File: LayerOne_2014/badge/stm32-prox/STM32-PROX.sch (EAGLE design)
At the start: 192 parts, among them IC1 IC_TPS6120X-QFN10, IC10 74XX244-OCTAL-TRISTATE-BUFFERS, IC105 MCP1824T-250, IC106 MCP1824T-120, IC11 CD4066, IC13 PQ1X331M2ZP-3V3-LDO-SOT-23-5, IC14 AD8052, IC2 STM32F103RET6, IC3 PQ1X331M2ZP-3V3-LDO-SOT-23-5, IC4 HCU-INVERTER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

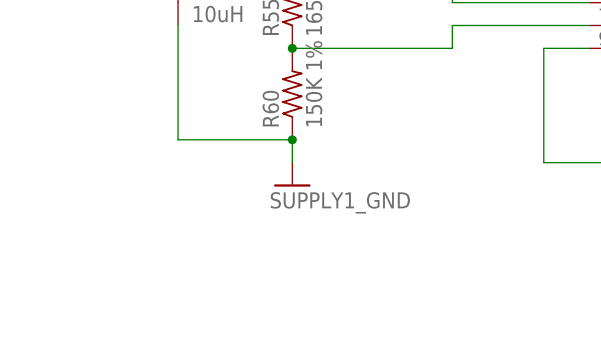
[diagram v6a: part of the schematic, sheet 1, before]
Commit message: 
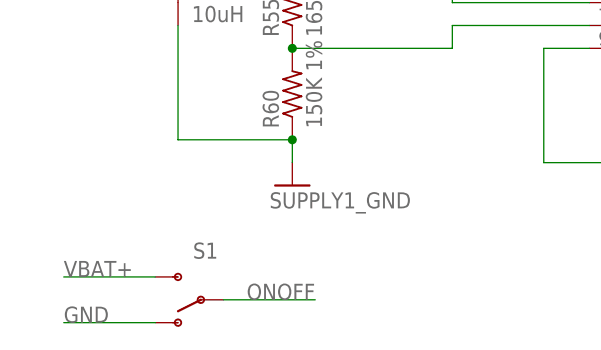
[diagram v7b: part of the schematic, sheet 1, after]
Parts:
- added S1: (no value), SparkFun-Electromechanical:SWITCH-SPDT-SMD-A
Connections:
- net GND: now also S1.O
- net ONOFF: now also S1.P
- net VBAT+: now also S1.S
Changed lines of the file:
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@@
 <part name="U$9" library="STM32-PROX" deviceset="BATT" device=""/>
 <part name="TP10" library="STM32-PROX" deviceset="--MERGED_TESTPAD" device="KEYSTONE-SMD" value="--MERGED_TESTPADKEYSTONE-SMD"/>
+<part name="S1" library="SparkFun-Electromechanical" deviceset="SWITCH-SPDT" device="-SMD-A"/>
 </parts>
 <sheets>
@@
 <instance part="U$9" gate="G$1" x="99.06" y="66.04"/>
 <instance part="TP10" gate="G$1" x="40.64" y="17.78"/>
+<instance part="S1" gate="1" x="-58.42" y="-25.4" rot="R180"/>
 </instances>
 <busses>
@@
 <wire x1="99.06" y1="60.96" x2="99.06" y2="53.34" width="0.1524" layer="91"/>
 <label x="101.6" y="55.88" size="1.778" layer="95"/>
+</segment>
+<segment>
+<pinref part="S1" gate="1" pin="S"/>
+<wire x1="-63.5" y1="-22.86" x2="-73.66" y2="-22.86" width="0.1524" layer="91"/>
+<label x="-73.66" y="-22.86" size="1.778" layer="95"/>
 </segment>
 </net>
@@
 <junction x="-48.26" y="-7.62"/>
 </segment>
+<segment>
+<pinref part="S1" gate="1" pin="O"/>
+<wire x1="-63.5" y1="-27.94" x2="-73.66" y2="-27.94" width="0.1524" layer="91"/>
+<label x="-73.66" y="-27.94" size="1.778" layer="95"/>
+</segment>
 </net>
 <net name="VBAT-" class="0">
@@
 <label x="-25.4" y="10.16" size="1.778" layer="95"/>
 </segment>
-</net>
+<segment>
+<pinref part="S1" gate="1" pin="P"/>
+<wire x1="-55.88" y1="-25.4" x2="-45.72" y2="-25.4" width="0.1524" layer="91"/>
+<label x="-53.34" y="-25.4" size="1.778" layer="95"/>
+</segment>
+</net>

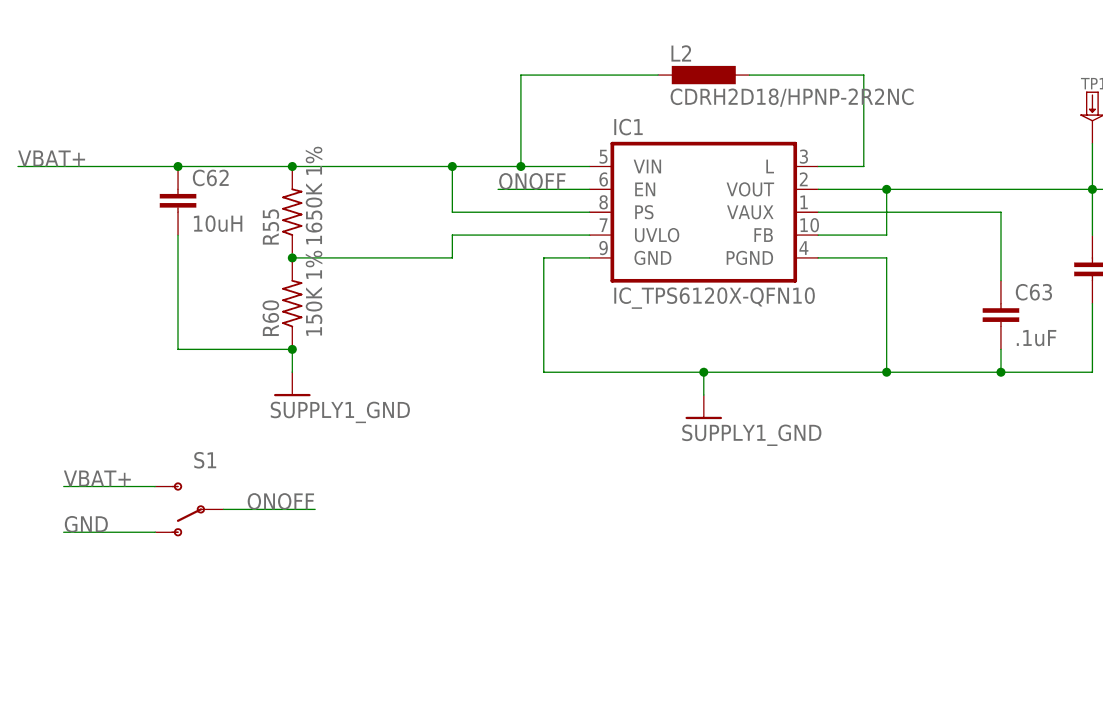
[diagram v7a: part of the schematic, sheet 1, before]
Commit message: 
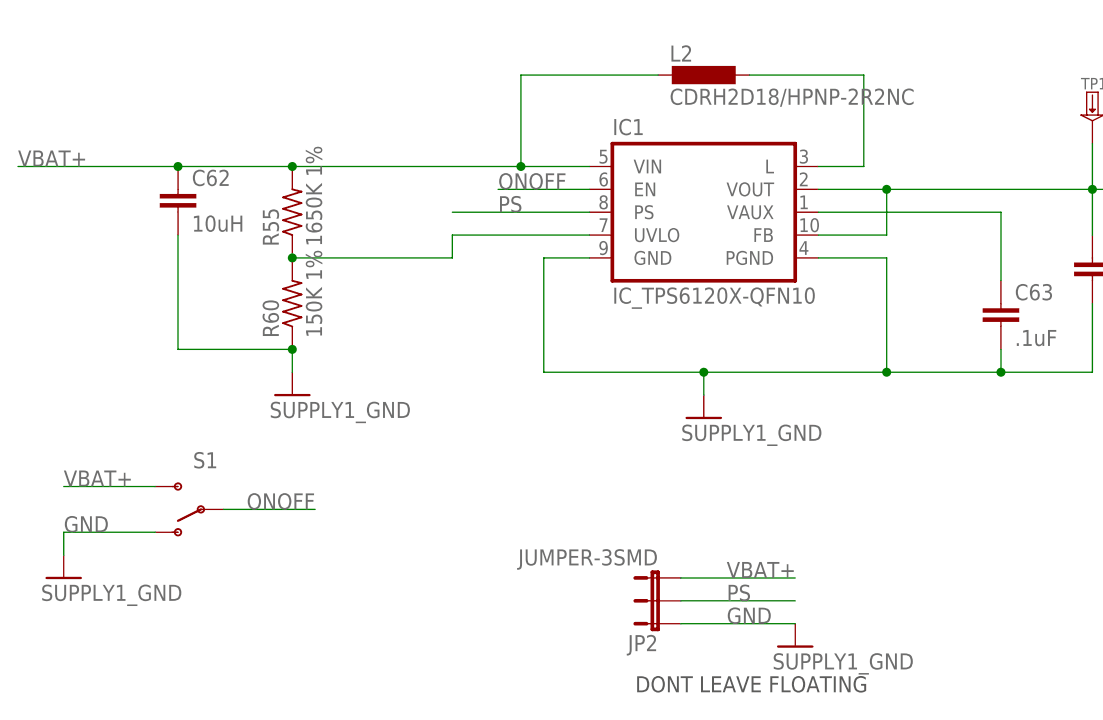
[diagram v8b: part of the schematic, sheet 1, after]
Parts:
- added JP2: JUMPER-3SMD, SparkFun-Passives:JUMPER-3SMD
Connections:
- new net PS: IC1IC.PS, JP2.2
- net GND: now also JP2.1
- net VBAT+: now also JP2.3; no longer IC1IC.PS
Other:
- note added: "DONT LEAVE FLOATING"
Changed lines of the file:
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@@
 <part name="TP10" library="STM32-PROX" deviceset="--MERGED_TESTPAD" device="KEYSTONE-SMD" value="--MERGED_TESTPADKEYSTONE-SMD"/>
 <part name="S1" library="SparkFun-Electromechanical" deviceset="SWITCH-SPDT" device="-SMD-A"/>
+<part name="GND20" library="badge.lbrbadge_2013" deviceset="SUPPLY1_GND" device=""/>
+<part name="JP2" library="SparkFun-Passives" deviceset="JUMPER-3" device="SMD"/>
+<part name="GND21" library="badge.lbrbadge_2013" deviceset="SUPPLY1_GND" device=""/>
 </parts>
 <sheets>
 <sheet>
 <plain>
+<text x="-10.16" y="-45.72" size="1.778" layer="97">DONT LEAVE FLOATING</text>
 </plain>
 <instances>
@@
 <instance part="TP10" gate="G$1" x="40.64" y="17.78"/>
 <instance part="S1" gate="1" x="-58.42" y="-25.4" rot="R180"/>
+<instance part="GND20" gate="1" x="-73.66" y="-33.02"/>
+<instance part="JP2" gate="G$1" x="-7.62" y="-38.1" rot="R90"/>
+<instance part="GND21" gate="1" x="7.62" y="-40.64"/>
 </instances>
 <busses>
@@
 <wire x1="-60.96" y1="12.7" x2="-78.74" y2="12.7" width="0.1524" layer="91"/>
 <junction x="-60.96" y="12.7"/>
-<pinref part="IC1" gate="IC" pin="PS"/>
-<wire x1="-15.24" y1="7.62" x2="-30.48" y2="7.62" width="0.1524" layer="91"/>
-<wire x1="-30.48" y1="7.62" x2="-30.48" y2="12.7" width="0.1524" layer="91"/>
-<junction x="-30.48" y="12.7"/>
 <pinref part="R55" gate="G$1" pin="2"/>
 <junction x="-48.26" y="12.7"/>
@@
 <wire x1="-63.5" y1="-22.86" x2="-73.66" y2="-22.86" width="0.1524" layer="91"/>
 <label x="-73.66" y="-22.86" size="1.778" layer="95"/>
+</segment>
+<segment>
+<pinref part="JP2" gate="G$1" pin="3"/>
+<wire x1="-5.08" y1="-33.02" x2="7.62" y2="-33.02" width="0.1524" layer="91"/>
+<label x="0" y="-33.02" size="1.778" layer="95"/>
 </segment>
 </net>
@@
 <wire x1="-63.5" y1="-27.94" x2="-73.66" y2="-27.94" width="0.1524" layer="91"/>
 <label x="-73.66" y="-27.94" size="1.778" layer="95"/>
+<pinref part="GND20" gate="1" pin="GND"/>
+<wire x1="-73.66" y1="-30.48" x2="-73.66" y2="-27.94" width="0.1524" layer="91"/>
+</segment>
+<segment>
+<pinref part="JP2" gate="G$1" pin="1"/>
+<wire x1="-5.08" y1="-38.1" x2="7.62" y2="-38.1" width="0.1524" layer="91"/>
+<label x="0" y="-38.1" size="1.778" layer="95"/>
+<pinref part="GND21" gate="1" pin="GND"/>
 </segment>
 </net>
@@
 </segment>
 </net>
+<net name="PS" class="0">
+<segment>
+<pinref part="IC1" gate="IC" pin="PS"/>
+<wire x1="-15.24" y1="7.62" x2="-30.48" y2="7.62" width="0.1524" layer="91"/>
+<label x="-25.4" y="7.62" size="1.778" layer="95"/>
+</segment>
+<segment>
+<pinref part="JP2" gate="G$1" pin="2"/>
+<wire x1="-5.08" y1="-35.56" x2="7.62" y2="-35.56" width="0.1524" layer="91"/>
+<label x="0" y="-35.56" size="1.778" layer="95"/>
+</segment>
+</net>
